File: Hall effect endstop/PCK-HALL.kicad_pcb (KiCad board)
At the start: 2 copper layers, 45 x 12.2 mm, 5 parts, among them IC1 TMAG5328A1ZQDBVR, J1 Conn_01x03

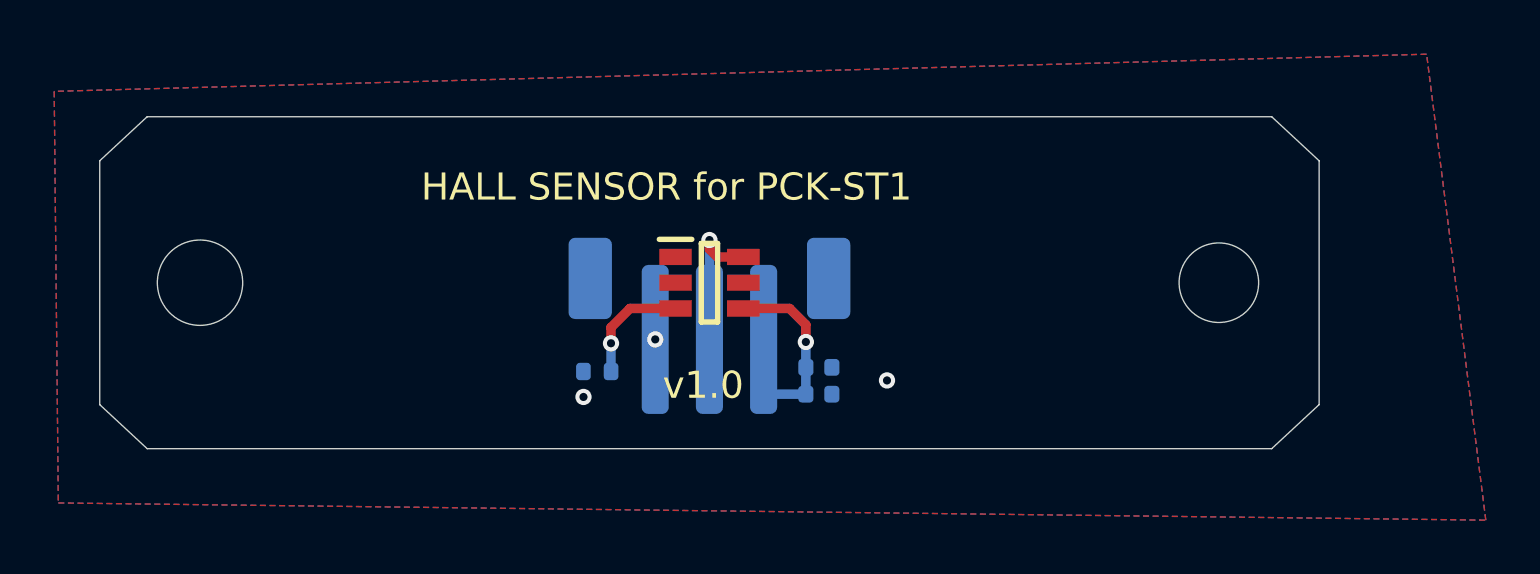
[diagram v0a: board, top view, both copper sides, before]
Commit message: Added JST PH connector 3D model to the design
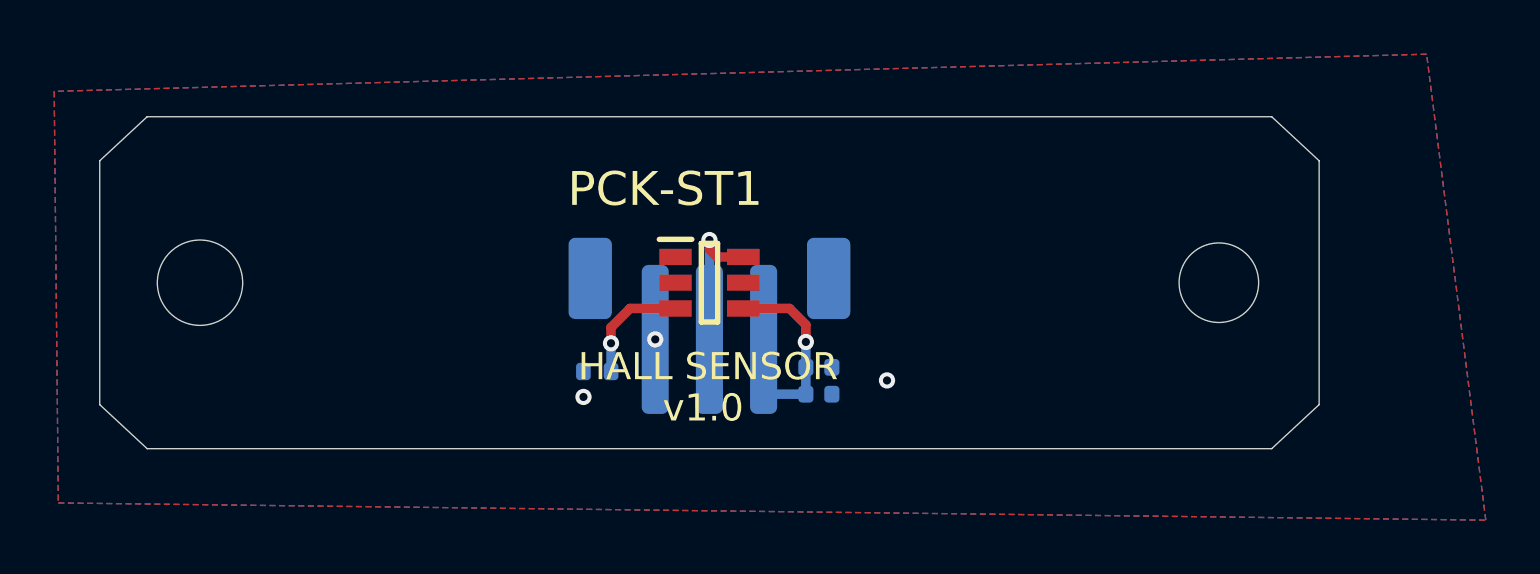
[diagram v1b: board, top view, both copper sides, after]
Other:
- board text added: "HALL SENSOR"
- board text added: "PCK-ST1"
- board text removed: "HALL SENSOR for PCK-ST1"
